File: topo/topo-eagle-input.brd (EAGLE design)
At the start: 68.6 x 53.3 mm, 59 parts, among them IC1 74HC04D, Q1 BSS138, Q2 PMV65XP, Q3 BSS138, Q4 BSS138, Q5 BSS138, Q6 BSS138, Q7 BSS138, Q8 BSS130, SW3 SWITCH_SPDT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

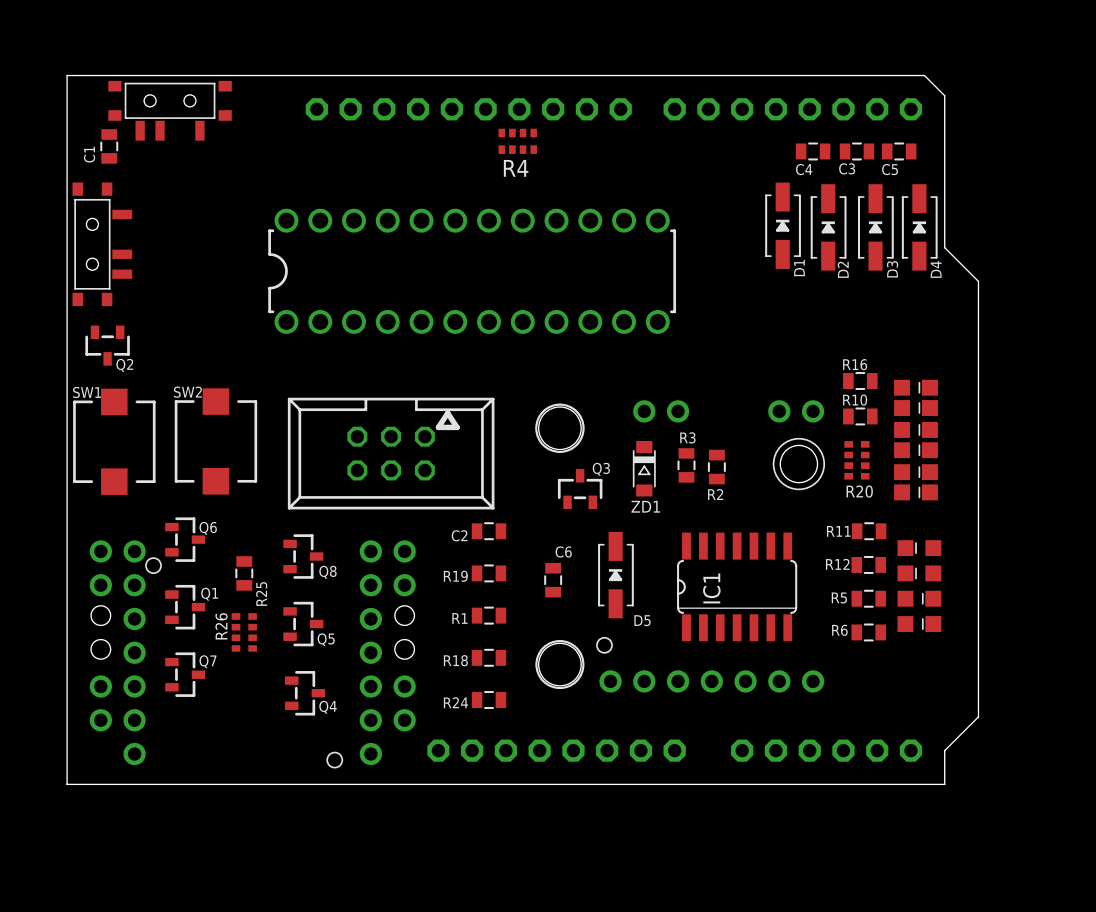
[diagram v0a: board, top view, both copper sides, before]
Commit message: changed board layout
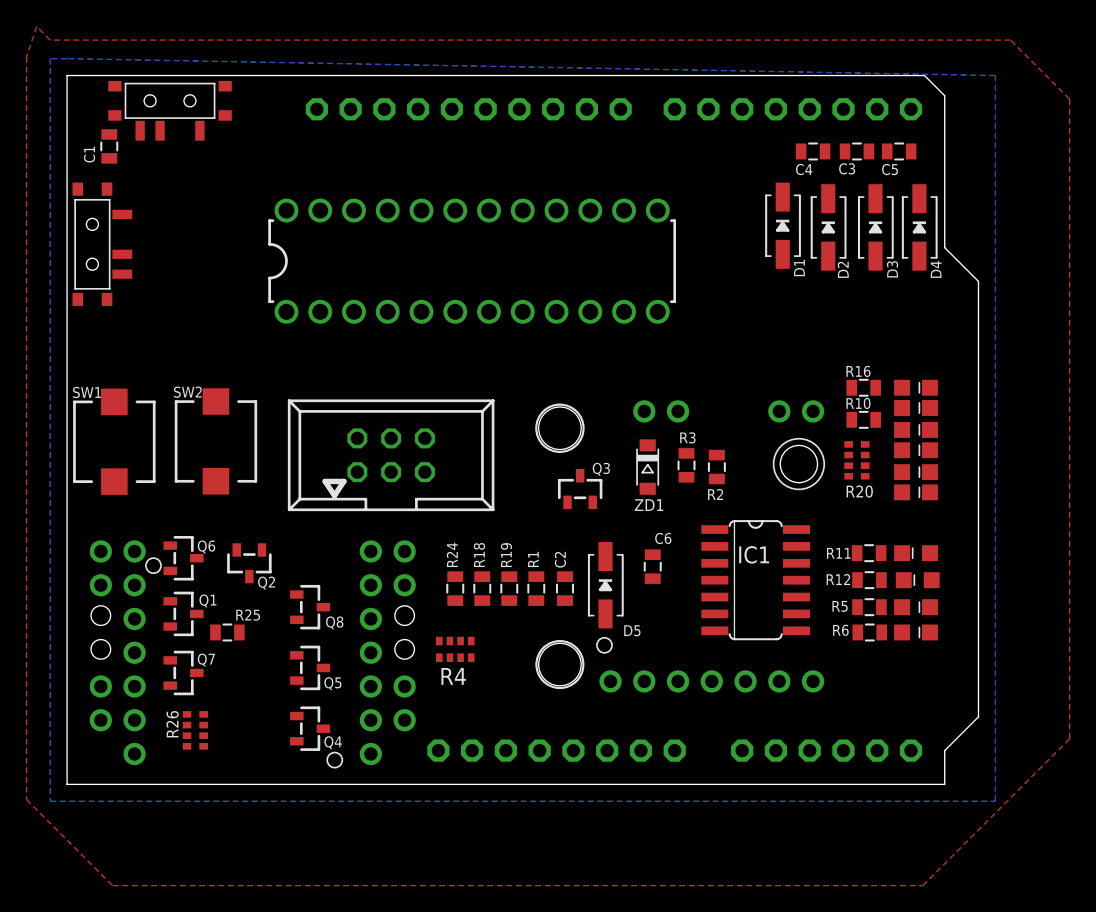
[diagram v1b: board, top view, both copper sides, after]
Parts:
- moved R4 38.5 mm to (29.2, 10.2)
- moved Q2 19.6 mm to (13.7, 16.6)
- moved R24 8.76 mm to (29.2, 14.7), turned to 270 degrees
- moved R26 8.24 mm to (9.65, 4.06)
- moved C6 7.56 mm to (44.1, 16.4)
- moved C2 7.16 mm to (37.5, 14.7), turned to 270 degrees
- moved R18 5.23 mm to (31.2, 14.7), turned to 90 degrees
- moved R25 4.62 mm to (12.1, 11.4), turned to 180 degrees
- moved R1 4.10 mm to (35.3, 14.7), turned to 270 degrees
- moved Q8 3.84 mm to (18.3, 13.3)
- moved Q5 3.34 mm to (18.3, 8.76)
- moved Q4 2.69 mm to (18.3, 4.19)
- moved R19 1.91 mm to (33.3, 14.7), turned to 90 degrees
- moved R11 1.65 mm to (60.4, 17.4)
- moved IC1 1.49 mm to (51.8, 15.4), turned to 270 degrees
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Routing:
- added copper zone on layer 1, net GND
- added copper zone on layer 16, net GND
